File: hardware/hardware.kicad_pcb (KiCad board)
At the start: 2 copper layers, 1 part, among them J1 Conn_02x03_Odd_Even

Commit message: feat: add resources
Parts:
- removed J1: Conn_02x03_Odd_Even, Connector_PinHeader_2.54mm:PinHeader_2x03_P2.54mm_Vertical_SMD
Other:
- board outline added: 49.7 x 46.9 mm

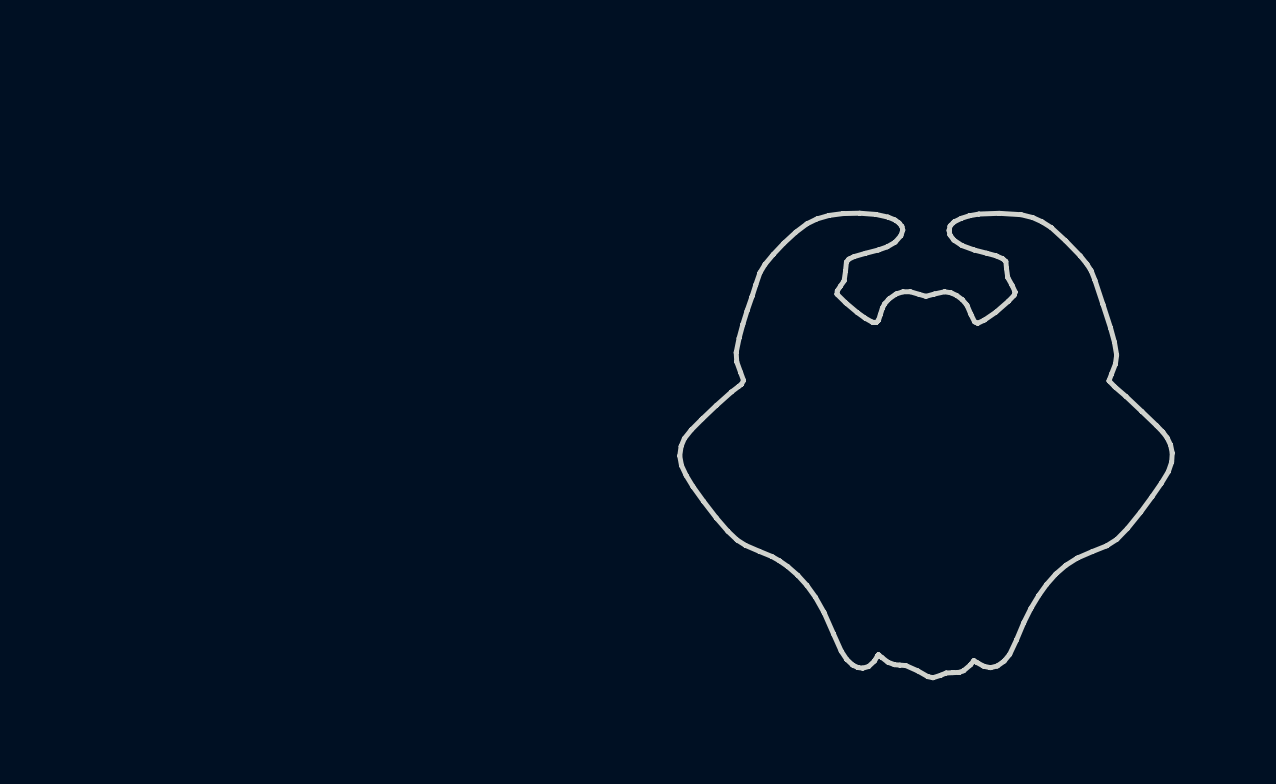
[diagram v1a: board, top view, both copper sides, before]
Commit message: feat: add zones with no cooper
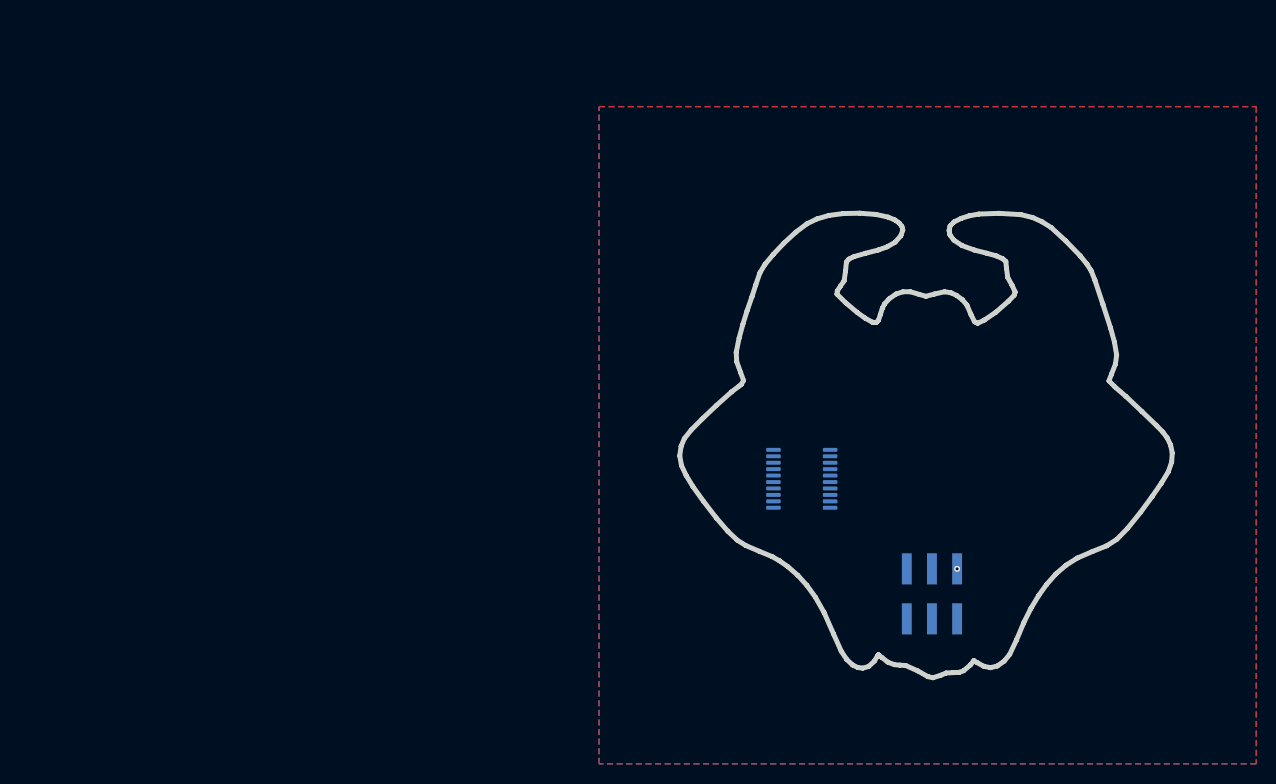
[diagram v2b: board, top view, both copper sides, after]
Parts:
- added J1: Conn_02x03_Odd_Even, Connector_PinHeader_2.54mm:PinHeader_2x03_P2.54mm_Vertical_SMD, B.Cu at (114.2, 77.4)
- added U1: CH32V003FxPx, Package_SO:TSSOP-20_4.4x6.5mm_P0.65mm, B.Cu at (101.0, 65.8)
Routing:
- net GND: vias 0 -> 1
- added copper zone on B.Cu, net GND
- added copper zone on F.Cu, net GND

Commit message: feat: add footprints
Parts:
- added Ref**: Val**, footprints:dots, F.Cu at (113.6, 59.7)
- added Ref**: Val**, footprints:front_eyes, F.Cu at (113.5, 62.5)
- added Ref**: Val**, footprints:drawing, F.Cu at (113.5, 62.5)
- moved U1 10.7 mm to (101.8, 55.1)
- moved J1 0.92 mm to (113.6, 76.7), turned to 90 degrees
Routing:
- net GND: vias 1 -> 0
